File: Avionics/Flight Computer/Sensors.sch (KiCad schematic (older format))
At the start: 12 parts, among them U5 MPU-9250, U7 LPS25HB

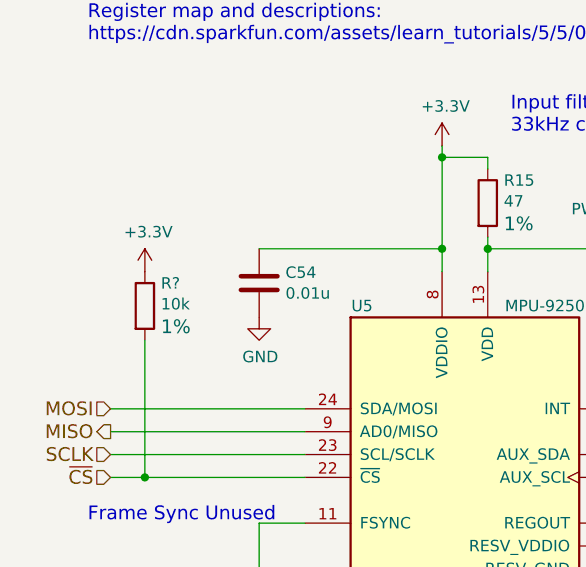
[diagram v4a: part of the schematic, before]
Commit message: Built outputs and added manufacturing part numbers to make BOM search easier.
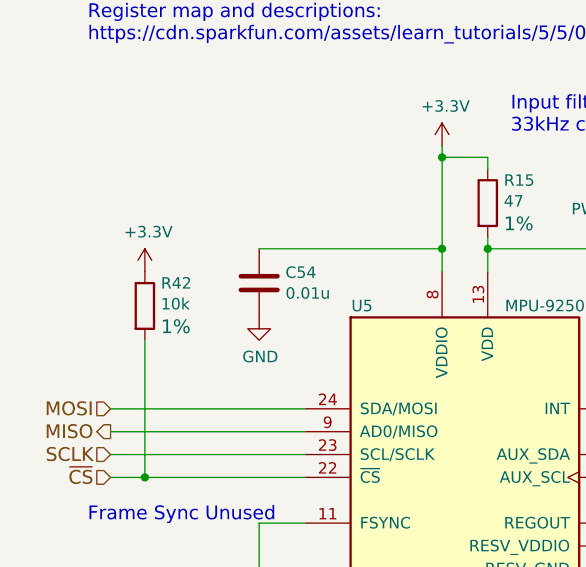
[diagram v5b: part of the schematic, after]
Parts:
- gave numbers to parts that had none: 1
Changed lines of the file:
@@
 $EndComp
 $Comp
-L GND #PWR120
+L GND #PWR0134
 U 1 1 58B4AF5E
 P 2400 5300
-F 0 "#PWR120" H -1950 1500 50  0001 C CNN
+F 0 "#PWR0134" H -1950 1500 50  0001 C CNN
 F 1 "GND" H 2405 5127 50  0000 C CNN
 F 2 "" H -1950 1750 50  0001 C CNN
@@
 $EndComp
 $Comp
-L +3.3V #PWR119
+L +3.3V #PWR0135
 U 1 1 58B4AFA2
 P 2300 2850
-F 0 "#PWR119" H -2200 -700 50  0001 C CNN
+F 0 "#PWR0135" H -2200 -700 50  0001 C CNN
 F 1 "+3.3V" H 2315 3023 50  0000 C CNN
 F 2 "" H -2200 -550 50  0001 C CNN
@@
 $EndComp
 $Comp
-L GND #PWR125
+L GND #PWR0136
 U 1 1 58B4B105
 P 8400 3550
-F 0 "#PWR125" H 4050 -250 50  0001 C CNN
+F 0 "#PWR0136" H 4050 -250 50  0001 C CNN
 F 1 "GND" H 8405 3377 50  0000 C CNN
 F 2 "" H 4050 0   50  0001 C CNN
@@
 Connection ~ 8400 3550
 $Comp
-L +3.3V #PWR126
+L +3.3V #PWR0137
 U 1 1 58B4B14B
 P 8450 1900
-F 0 "#PWR126" H 3950 -1650 50  0001 C CNN
+F 0 "#PWR0137" H 3950 -1650 50  0001 C CNN
 F 1 "+3.3V" H 8465 2073 50  0000 C CNN
 F 2 "" H 3950 -1500 50  0001 C CNN
@@
 Connection ~ 8450 2350
 $Comp
-L GND #PWR127
+L GND #PWR0138
 U 1 1 58B4B9E9
 P 9050 2700
-F 0 "#PWR127" H 4700 -1100 50  0001 C CNN
+F 0 "#PWR0138" H 4700 -1100 50  0001 C CNN
 F 1 "GND" H 9055 2527 50  0000 C CNN
 F 2 "" H 4700 -850 50  0001 C CNN
@@
 Input filter to reduce sensor reference noise. \n1.5kHz cutoff, 25uA bias current worst case
 $Comp
-L +3.3V #PWR124
+L +3.3V #PWR0139
 U 1 1 58B4C158
 P 7450 2100
-F 0 "#PWR124" H 2950 -1450 50  0001 C CNN
+F 0 "#PWR0139" H 2950 -1450 50  0001 C CNN
 F 1 "+3.3V" H 7465 2273 50  0000 C CNN
 F 2 "" H 2950 -1300 50  0001 C CNN
@@
 	3100 4500 3850 4500
 $Comp
-L GND #PWR123
+L GND #PWR0140
 U 1 1 58B4FB3E
 P 3850 4800
-F 0 "#PWR123" H -500 1000 50  0001 C CNN
+F 0 "#PWR0140" H -500 1000 50  0001 C CNN
 F 1 "GND" H 3855 4627 50  0000 C CNN
 F 2 "" H -500 1250 50  0001 C CNN
@@
 	3500 4800 3500 4750
 $Comp
-L +3.3V #PWR122
+L +3.3V #PWR0141
 U 1 1 58B50137
 P 3500 4750
-F 0 "#PWR122" H -1000 1200 50  0001 C CNN
+F 0 "#PWR0141" H -1000 1200 50  0001 C CNN
 F 1 "+3.3V" H 3515 4923 50  0000 C CNN
 F 2 "" H -1000 1350 50  0001 C CNN
@@
 IMU-INT
 $Comp
-L GND #PWR121
+L GND #PWR0142
 U 1 1 58B505FC
 P 3350 3600
-F 0 "#PWR121" H -1000 -200 50  0001 C CNN
+F 0 "#PWR0142" H -1000 -200 50  0001 C CNN
 F 1 "GND" H 3355 3427 50  0000 C CNN
 F 2 "" H -1000 50  50  0001 C CNN
@@
 Input filter to reduce sensor reference noise. \n33kHz cutoff, 3.5mA bias current worst case
 $Comp
-L GND #PWR118
+L GND #PWR0143
 U 1 1 58B50B96
 P 1500 3600
-F 0 "#PWR118" H -2850 -200 50  0001 C CNN
+F 0 "#PWR0143" H -2850 -200 50  0001 C CNN
 F 1 "GND" H 1505 3427 50  0000 C CNN
 F 2 "" H -2850 50  50  0001 C CNN
@@
 NoConn ~ 8000 3200
 $Comp
-L PWR_FLAG #FLG17
+L PWR_FLAG #FLG0144
 U 1 1 58BF1DC3
 P 3050 3300
-F 0 "#FLG17" H -1800 125 50  0001 C CNN
+F 0 "#FLG0144" H -1800 125 50  0001 C CNN
 F 1 "PWR_FLAG" H 3050 3474 50  0000 C CNN
 F 2 "" H -1800 50  50  0001 C CNN
@@
 Connection ~ 3050 3300
 $Comp
-L PWR_FLAG #FLG18
+L PWR_FLAG #FLG0145
 U 1 1 58BF1E5B
 P 8900 2350
-F 0 "#FLG18" H 4050 -825 50  0001 C CNN
+F 0 "#FLG0145" H 4050 -825 50  0001 C CNN
 F 1 "PWR_FLAG" H 8900 2524 50  0000 C CNN
 F 2 "" H 4050 -900 50  0001 C CNN
@@
 Connection ~ 8500 3550
 $Comp
-L R R?
+L R R42
 U 1 1 58D7F4C9
 P 1000 3550
-F 0 "R?" H 1070 3649 50  0000 L CNN
+F 0 "R42" H 1070 3649 50  0000 L CNN
 F 1 "10k" H 1070 3558 50  0000 L CNN
 F 2 "Resistors_SMD:R_0402" V -6450 1900 50  0001 C CNN
@@
 $EndComp
 $Comp
-L +3.3V #PWR?
+L +3.3V #PWR0146
 U 1 1 58D7F763
 P 1000 3400
-F 0 "#PWR?" H -3500 -150 50  0001 C CNN
+F 0 "#PWR0146" H -3500 -150 50  0001 C CNN
 F 1 "+3.3V" H 1015 3573 50  0000 C CNN
 F 2 "" H -3500 0   50  0001 C CNN

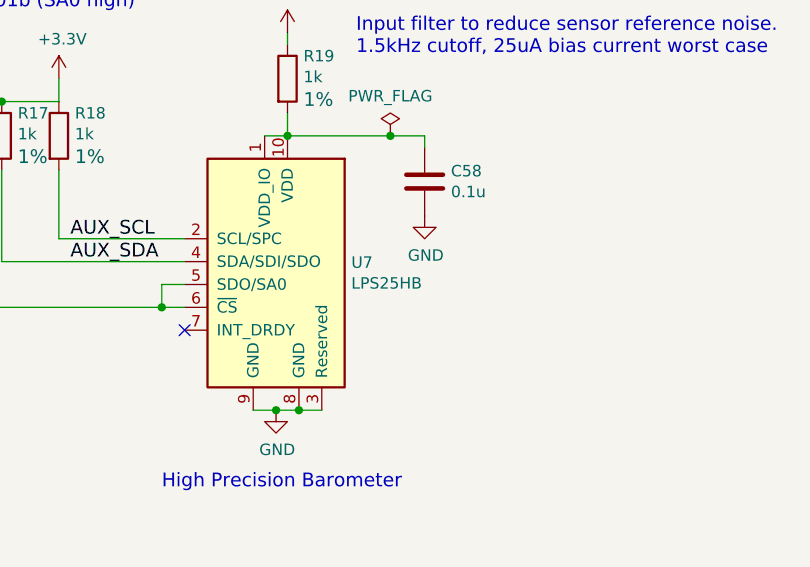
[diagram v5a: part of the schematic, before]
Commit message: Updated more manufacturing part numbers for macrofab compatibility.
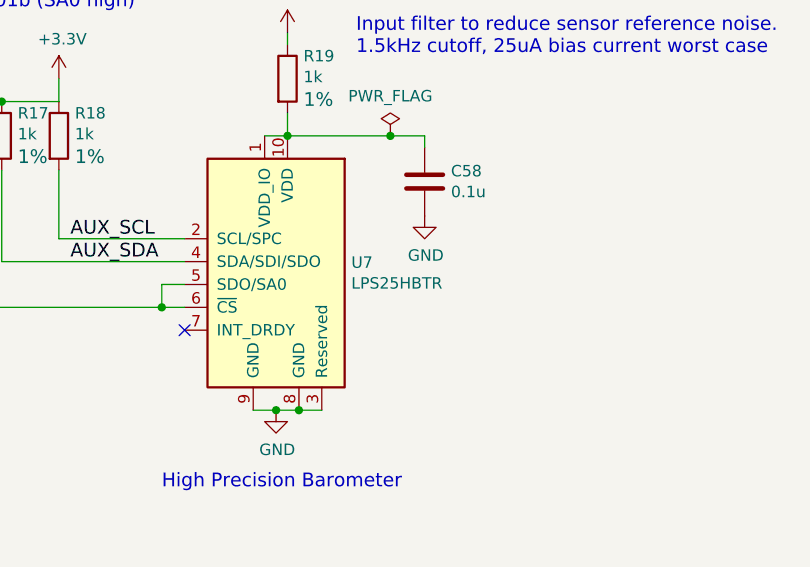
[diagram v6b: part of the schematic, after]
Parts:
- U7: value LPS25HB -> LPS25HBTR
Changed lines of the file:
@@
 P 8400 2950
 F 0 "U7" H 8071 2996 50  0000 R CNN
-F 1 "LPS25HB" H 8071 2905 50  0000 R CNN
+F 1 "LPS25HBTR" H 8071 2905 50  0000 R CNN
 F 2 "Housings_LGA:HLGA-10L_2.5x2.5mm_Pitch0.6mm" H -1250 1100 50  0001 C CIN
 F 3 "http://www.st.com/resource/en/datasheet/lps25hb.pdf" H -1250 1200 50  0001 C CNN
